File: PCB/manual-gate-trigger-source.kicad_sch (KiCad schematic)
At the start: 53 parts

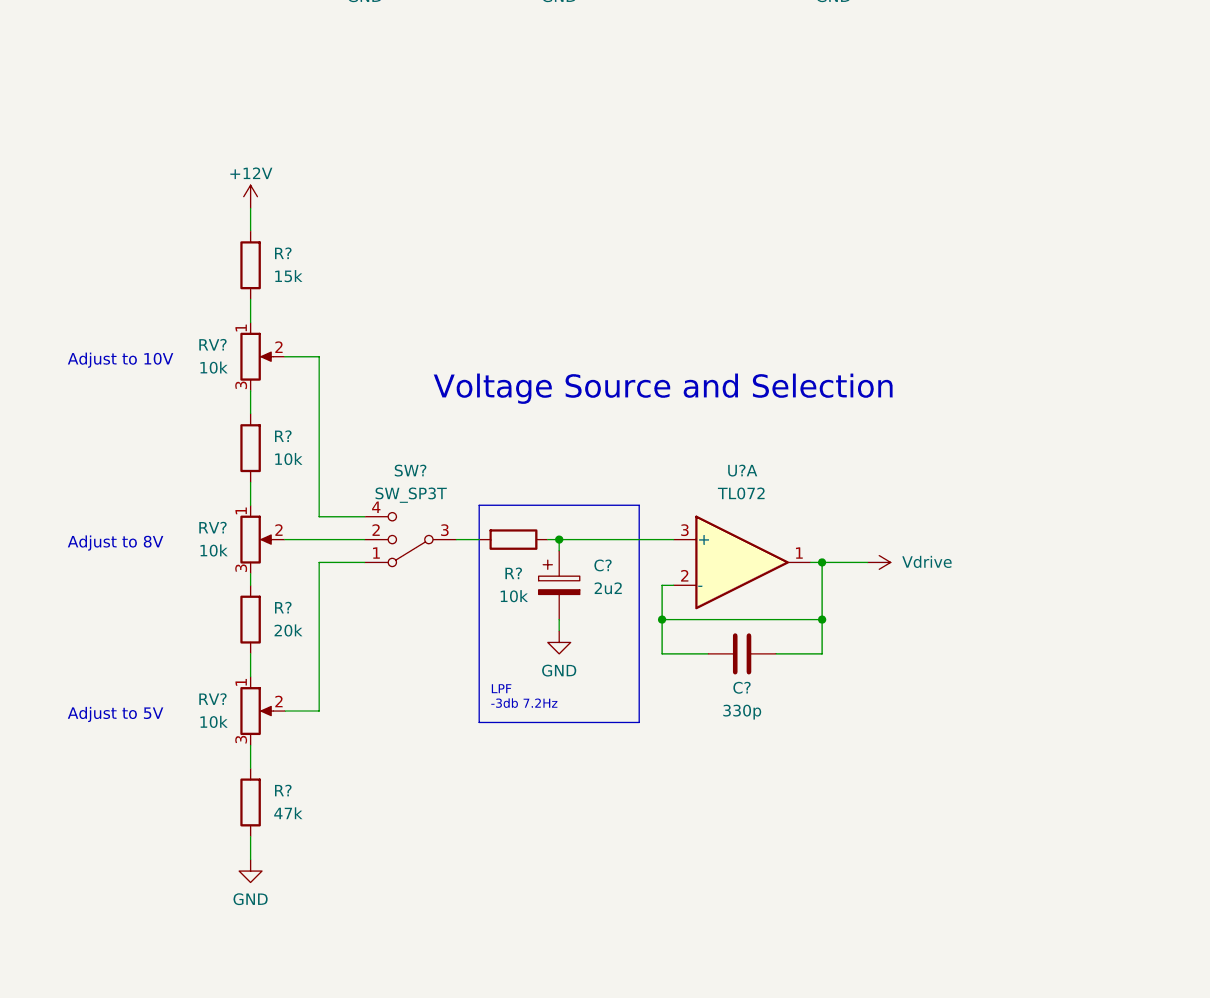
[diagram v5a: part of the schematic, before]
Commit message: :art: Improve the voltage selector circuit
Use parallel resistors to the upper/lower leg of an 8V divider to switch
between 5V and 10V with a SPDT switch with middle off position

Fixes: #4
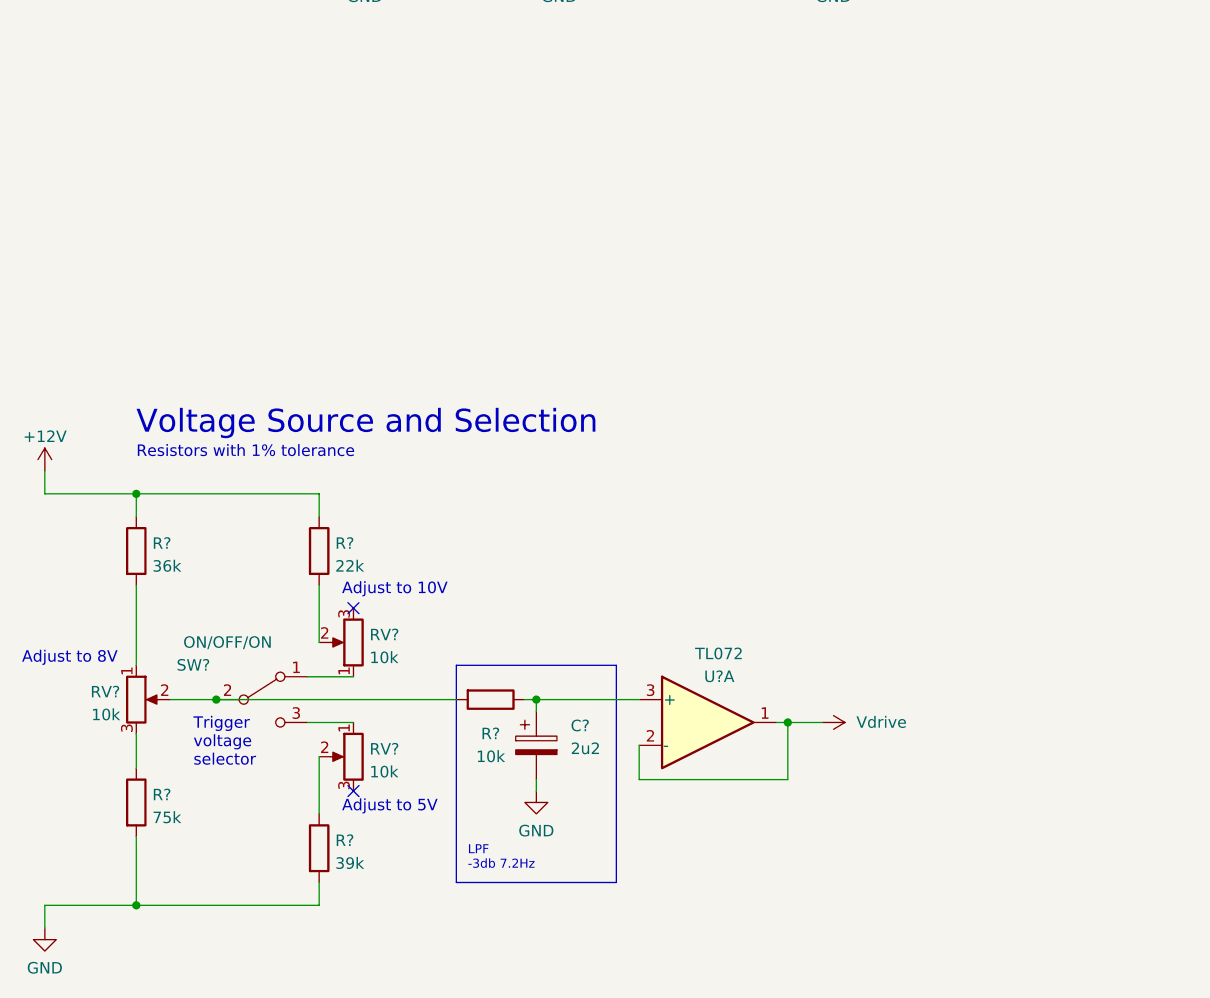
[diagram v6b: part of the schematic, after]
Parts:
- removed C?: 330p, symbol Device:C
- removed R?: 15k, symbol Device:R
- removed R?: 10k, symbol Device:R
- removed R?: 20k, symbol Device:R
- removed R?: 47k, symbol Device:R
- removed RV? (x3): 10k, symbol Device:R_Potentiometer
- removed SW?: SW_SP3T, symbol Switch:SW_SP3T
- added R?: 22k, symbol Device:R
- added R?: 75k, symbol Device:R
- added R?: 39k, symbol Device:R
- added R?: 36k, symbol Device:R
- added RV? (x3): 10k, symbol Device:R_Potentiometer
- added SW?: ON/OFF/ON, symbol Switch:SW_SPDT
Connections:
- net +12V: now also R?.1, R?.1
- net GND: now also R?.2, R?.2
- net at R?.2: now also RV?.2, SW?.2 (B)
- new net: RV?.1, SW?.1 (A)
- new net: R?.2, RV?.2
- new net: RV?.1, SW?.3 (C)
- new net: R?.1, RV?.2
- new net: R?.2, RV?.1
- new net: R?.1, RV?.3
- no-connect marks 2 -> 4
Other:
- note added: "Resistors with 1% tolerance"
- note added: "Trigger voltage selector"
- moved on the sheet: C?, R?, U?A

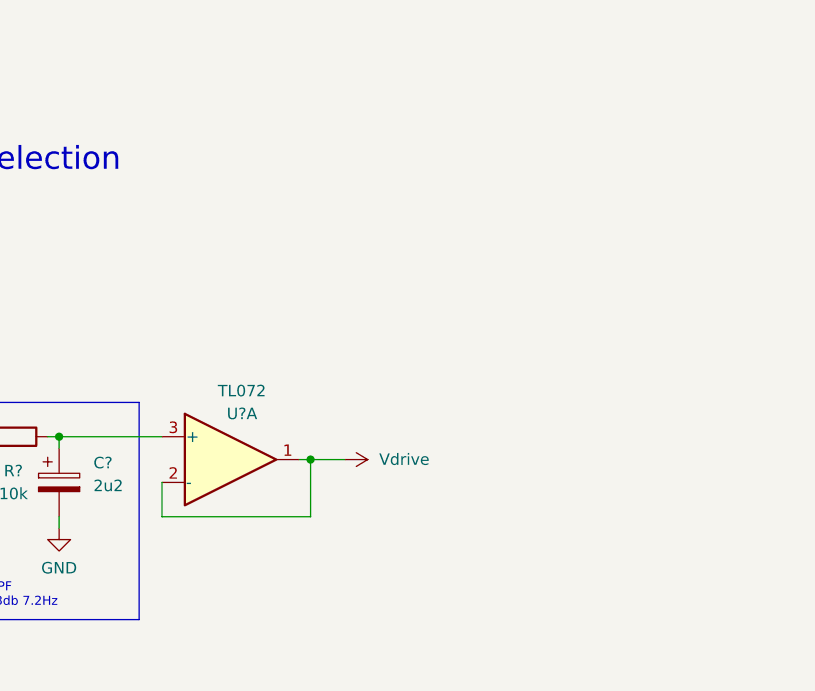
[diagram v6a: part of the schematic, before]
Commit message: :sparkles: Add a drive transistor to the voltage source
The op-amp alone cannot drive all outputs. Add a transistor as output driver
and incorporate it into the feedback loop.
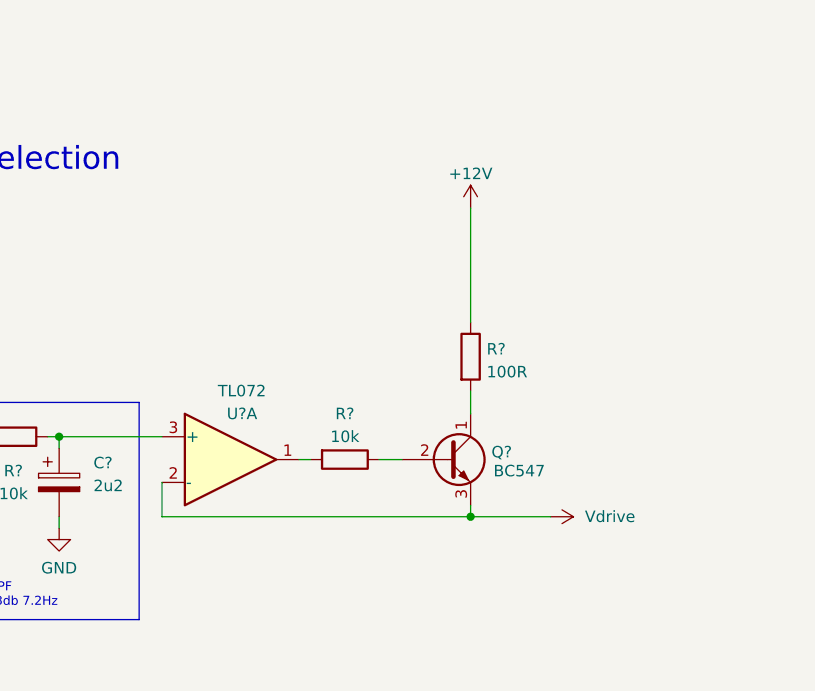
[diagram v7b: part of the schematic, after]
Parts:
- added Q?: BC547, Package_TO_SOT_THT:TO-92_Inline, symbol Transistor_BJT:BC547
- added R?: 10k, symbol Device:R
- added R?: 100R, symbol Device:R
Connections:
- net +12V: now also R?.1
- net Vdrive: now also Q?.3 (E); no longer U?.1
- new net: Q?.2 (B), R?.1
- new net: R?.2, U?.1
- new net: Q?.1 (C), R?.2
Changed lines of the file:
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@@
   (junction (at 198.12 146.05) (diameter 0) (color 0 0 0 0)
   )
+  (junction (at 116.84 175.26) (diameter 0) (color 0 0 0 0)
+  )
   (junction (at 232.41 130.81) (diameter 0) (color 0 0 0 0)
   )
@@
   )
   (junction (at 54.61 45.72) (diameter 0) (color 0 0 0 0)
-  )
-  (junction (at 99.06 168.91) (diameter 0) (color 0 0 0 0)
   )
   (junction (at 26.67 189.23) (diameter 0) (color 0 0 0 0)
@@
     (stroke (width 0) (type default) (color 0 0 0 0))
   )
+  (wire (pts (xy 116.84 173.99) (xy 116.84 175.26))
+    (stroke (width 0) (type default) (color 0 0 0 0))
+  )
   (wire (pts (xy 168.91 135.89) (xy 167.64 135.89))
     (stroke (width 0) (type default) (color 0 0 0 0))
@@
     (stroke (width 0) (type default) (color 0 0 0 0))
   )
+  (wire (pts (xy 116.84 175.26) (xy 125.73 175.26))
+    (stroke (width 0) (type default) (color 0 0 0 0))
+  )
   (wire (pts (xy 138.43 63.5) (xy 138.43 69.85))
     (stroke (width 0) (type default) (color 0 0 0 0))
@@
     (stroke (width 0) (type default) (color 0 0 0 0))
   )
+  (wire (pts (xy 106.68 168.91) (xy 109.22 168.91))
+    (stroke (width 0) (type default) (color 0 0 0 0))
+  )
   (wire (pts (xy 73.66 78.74) (xy 73.66 81.28))
     (stroke (width 0) (type default) (color 0 0 0 0))
@@
   )
   (wire (pts (xy 35.56 166.37) (xy 62.23 166.37))
+    (stroke (width 0) (type default) (color 0 0 0 0))
+  )
+  (wire (pts (xy 116.84 140.97) (xy 116.84 153.67))
     (stroke (width 0) (type default) (color 0 0 0 0))
   )
@@
     (stroke (width 0) (type default) (color 0 0 0 0))
   )
-  (wire (pts (xy 99.06 168.91) (xy 102.87 168.91))
-    (stroke (width 0) (type default) (color 0 0 0 0))
-  )
   (polyline (pts (xy 62.23 162.56) (xy 80.01 162.56))
     (stroke (width 0) (type default) (color 0 0 0 0))
@@
     (stroke (width 0) (type default) (color 0 0 0 0))
   )
-  (wire (pts (xy 82.55 175.26) (xy 99.06 175.26))
+  (wire (pts (xy 82.55 175.26) (xy 116.84 175.26))
     (stroke (width 0) (type default) (color 0 0 0 0))
   )
@@
     (stroke (width 0) (type default) (color 0 0 0 0))
   )
+  (wire (pts (xy 116.84 161.29) (xy 116.84 163.83))
+    (stroke (width 0) (type default) (color 0 0 0 0))
+  )
   (polyline (pts (xy 92.71 53.34) (xy 96.52 53.34))
     (stroke (width 0) (type solid) (color 0 0 0 0))
@@
   )
   (wire (pts (xy 30.48 166.37) (xy 35.56 166.37))
-    (stroke (width 0) (type default) (color 0 0 0 0))
-  )
-  (wire (pts (xy 99.06 175.26) (xy 99.06 168.91))
     (stroke (width 0) (type default) (color 0 0 0 0))
   )
@@
     (pin "1")
     (pin "2")
+  )
+  (symbol (lib_id "power:+12V") (at 116.84 140.97 0) (unit 1)
+    (in_bom yes) (on_board yes)
+    (property "Reference" "#PWR?" (id 0) (at 116.84 144.78 0)
+      (effects (font (size 1.27 1.27)) hide)
+    )
+    (property "Value" "+12V" (id 1) (at 116.84 137.16 0))
+    (property "Footprint" "" (id 2) (at 116.84 140.97 0)
+      (effects (font (size 1.27 1.27)) hide)
+    )
+    (property "Datasheet" "" (id 3) (at 116.84 140.97 0)
+      (effects (font (size 1.27 1.27)) hide)
+    )
+    (pin "1")
   )
   (symbol (lib_id "power:GND") (at 250.19 87.63 0) (unit 1)
@@
     (pin "1")
   )
+  (symbol (lib_id "Device:R") (at 102.87 168.91 270) (unit 1)
+    (in_bom yes) (on_board yes)
+    (property "Reference" "R?" (id 0) (at 102.87 163.83 90))
+    (property "Value" "10k" (id 1) (at 102.87 166.37 90))
+    (property "Footprint" "" (id 2) (at 102.87 167.132 90)
+      (effects (font (size 1.27 1.27)) hide)
+    )
+    (property "Datasheet" "~" (id 3) (at 102.87 168.91 0)
+      (effects (font (size 1.27 1.27)) hide)
+    )
+    (pin "1")
+    (pin "2")
+  )
   (symbol (lib_id "Device:R") (at 256.54 66.04 90) (unit 1)
     (in_bom yes) (on_board yes)
@@
     (pin "1")
   )
+  (symbol (lib_id "Device:R") (at 116.84 157.48 0) (unit 1)
+    (in_bom yes) (on_board yes) (fields_autoplaced)
+    (property "Reference" "R?" (id 0) (at 118.618 156.6453 0)
+      (effects (font (size 1.27 1.27)) (justify left))
+    )
+    (property "Value" "100R" (id 1) (at 118.618 159.1822 0)
+      (effects (font (size 1.27 1.27)) (justify left))
+    )
+    (property "Footprint" "" (id 2) (at 115.062 157.48 90)
+      (effects (font (size 1.27 1.27)) hide)
+    )
+    (property "Datasheet" "~" (id 3) (at 116.84 157.48 0)
+      (effects (font (size 1.27 1.27)) hide)
+    )
+    (pin "1")
+    (pin "2")
+  )
   (symbol (lib_id "Device:R") (at 59.69 73.66 90) (unit 1)
     (in_bom yes) (on_board yes) (fields_autoplaced)
@@
     (pin "T")
     (pin "TN")
+  )
+  (symbol (lib_id "Transistor_BJT:BC547") (at 114.3 168.91 0) (unit 1)
+    (in_bom yes) (on_board yes)
+    (property "Reference" "Q?" (id 0) (at 119.1514 168.0753 0)
+      (effects (font (size 1.27 1.27)) (justify left))
+    )
+    (property "Value" "BC547" (id 1) (at 119.38 170.18 0)
+      (effects (font (size 1.27 1.27)) (justify left))
+    )
+    (property "Footprint" "Package_TO_SOT_THT:TO-92_Inline" (id 2) (at 119.38 170.815 0)
+      (effects (font (size 1.27 1.27) italic) (justify left) hide)
+    )
+    (property "Datasheet" "https://www.onsemi.com/pub/Collateral/BC550-D.pdf" (id 3) (at 114.3 168.91 0)
+      (effects (font (size 1.27 1.27)) (justify left) hide)
+    )
+    (pin "1")
+    (pin "2")
+    (pin "3")
   )
   (symbol (lib_id "Device:R") (at 46.99 182.88 0) (unit 1)
@@
     (pin "2")
   )
-  (symbol (lib_id "power:Vdrive") (at 102.87 168.91 270) (unit 1)
-    (in_bom yes) (on_board yes) (fields_autoplaced)
-    (property "Reference" "#PWR?" (id 0) (at 99.06 163.83 0)
-      (effects (font (size 1.27 1.27)) hide)
-    )
-    (property "Value" "Vdrive" (id 1) (at 106.68 168.9099 90)
-      (effects (font (size 1.27 1.27)) (justify left))
-    )
-    (property "Footprint" "" (id 2) (at 102.87 168.91 0)
-      (effects (font (size 1.27 1.27)) hide)
-    )
-    (property "Datasheet" "" (id 3) (at 102.87 168.91 0)
+  (symbol (lib_id "power:Vdrive") (at 125.73 175.26 270) (unit 1)
+    (in_bom yes) (on_board yes) (fields_autoplaced)
+    (property "Reference" "#PWR?" (id 0) (at 121.92 170.18 0)
+      (effects (font (size 1.27 1.27)) hide)
+    )
+    (property "Value" "Vdrive" (id 1) (at 129.54 175.2599 90)
+      (effects (font (size 1.27 1.27)) (justify left))
+    )
+    (property "Footprint" "" (id 2) (at 125.73 175.26 0)
+      (effects (font (size 1.27 1.27)) hide)
+    )
+    (property "Datasheet" "" (id 3) (at 125.73 175.26 0)
       (effects (font (size 1.27 1.27)) hide)
     )
@@
       (reference "#PWR?") (unit 1) (value "GND") (footprint "")
     )
+    (path "/1ae3faff-2a27-428e-abae-d3be6c4066d8"
+      (reference "#PWR?") (unit 1) (value "+12V") (footprint "")
+    )
     (path "/22c0a682-9532-4c74-84e6-cd37a121d21b"
       (reference "#PWR?") (unit 1) (value "GND") (footprint "")
@@
       (reference "Q?") (unit 1) (value "BC547") (footprint "Package_TO_SOT_THT:TO-92_Inline")
     )
+    (path "/d78e7427-60e8-44f0-aab7-63b1109c15e8"
+      (reference "Q?") (unit 1) (value "BC547") (footprint "Package_TO_SOT_THT:TO-92_Inline")
+    )
     (path "/081adf09-cddd-4e13-b289-4b685255adec"
       (reference "R?") (unit 1) (value "10k") (footprint "")
@@
       (reference "R?") (unit 1) (value "75k") (footprint "")
     )
+    (path "/c50d62f7-e042-4438-bc62-37137c598198"
+      (reference "R?") (unit 1) (value "10k") (footprint "")
+    )
     (path "/c7af4d99-9e2b-4d8a-80e7-cea49430b108"
       (reference "R?") (unit 1) (value "1k") (footprint "")
     )
+    (path "/ce2871eb-2b71-4d11-a74e-15aab68563ca"
+      (reference "R?") (unit 1) (value "100R") (footprint "")
+    )
     (path "/ceca7e89-cc8e-4e4d-a7a5-87d63d1be391"

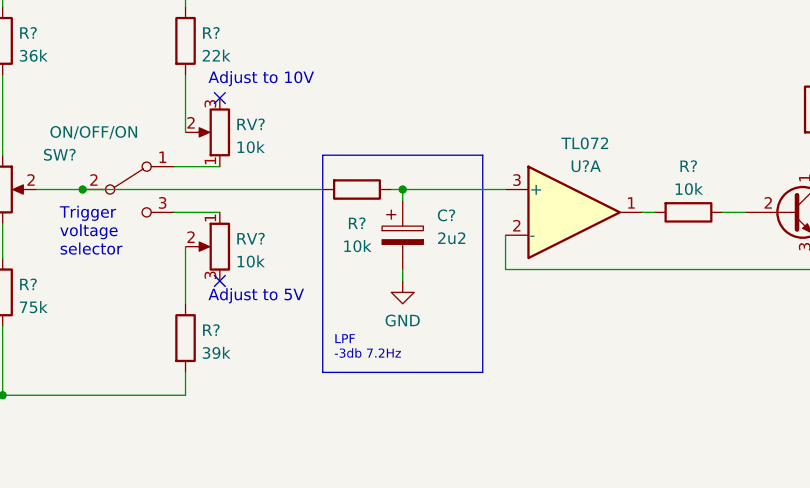
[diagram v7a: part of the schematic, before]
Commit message: :wrench: Adjust LPF for then voltage selector switch
Measurements have shown that this is the best value for the switch that
will most likely be used.
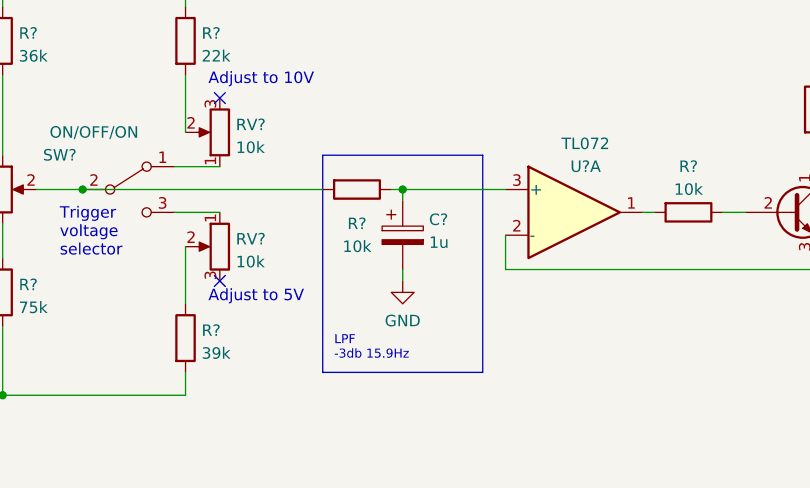
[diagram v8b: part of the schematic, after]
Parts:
- C?: value 2u2 -> 1u
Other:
- note added: "LPF -3db 15.9Hz"
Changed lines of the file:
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@@
     (effects (font (size 1 1)) (justify left bottom))
   )
-  (text "LPF\n-3db 7.2Hz" (at 63.5 185.42 0)
+  (text "LPF\n-3db 15.9Hz" (at 63.5 185.42 0)
     (effects (font (size 1 1)) (justify left bottom))
   )
@@
   (symbol (lib_id "Device:C_Polarized") (at 71.12 171.45 0) (unit 1)
     (in_bom yes) (on_board yes) (fields_autoplaced)
-    (property "Reference" "C?" (id 0) (at 74.93 169.2909 0)
-      (effects (font (size 1.27 1.27)) (justify left))
-    )
-    (property "Value" "2u2" (id 1) (at 74.93 171.8309 0)
+    (property "Reference" "C?" (id 0) (at 74.041 169.7263 0)
+      (effects (font (size 1.27 1.27)) (justify left))
+    )
+    (property "Value" "1u" (id 1) (at 74.041 172.2632 0)
       (effects (font (size 1.27 1.27)) (justify left))
     )
@@
     )
     (path "/54786b45-0837-4756-b25c-b9d34819286c"
-      (reference "C?") (unit 1) (value "2u2") (footprint "")
+      (reference "C?") (unit 1) (value "1u") (footprint "")
     )
     (path "/55ae8d37-694d-4ee7-b088-64f880e72069"
